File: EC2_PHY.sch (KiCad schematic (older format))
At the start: 72 parts

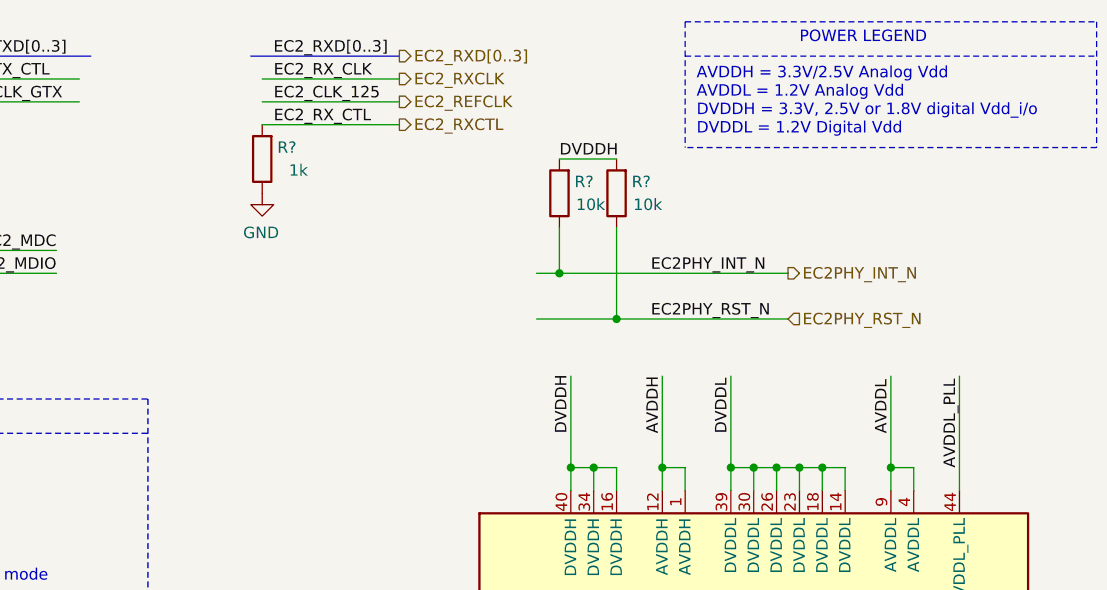
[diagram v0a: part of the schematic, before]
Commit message: Fix reset signal path
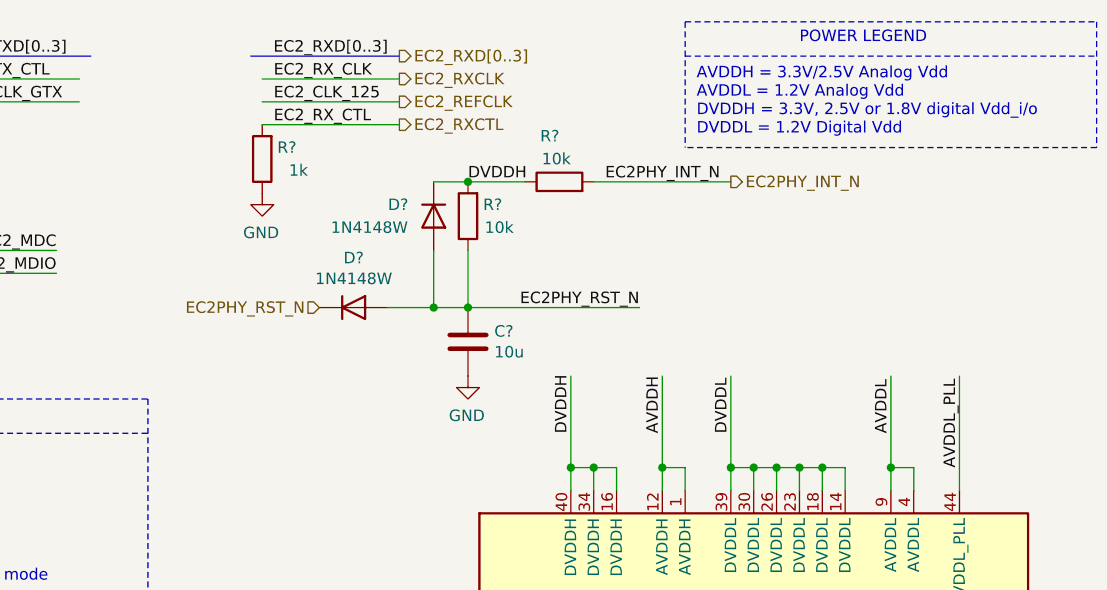
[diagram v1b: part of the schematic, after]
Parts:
- removed R? (x2): 10k, symbol Device:R
- added C?: 10u, symbol Device:C
- added D? (x2): 1N4148W, Diode_SMD:D_SOD-123, symbol Diode:1N4148W
- added R? (x2): 10k, symbol Device:R
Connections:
- wire segments 220 -> 221
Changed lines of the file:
@@
 $Descr A4 11693 8268
 encoding utf-8
-Sheet 16 28
+Sheet 14 28
 Title "DJANGO"
 Date "2020-12-06"
@@
 Text Label 3000 5050 0    50   ~ 0
 EC2PHY_INT_N
-Text Label 4450 1600 0    50   ~ 0
+Text Label 4250 1200 0    50   ~ 0
 EC2PHY_INT_N
-Text HLabel 5050 1600 2    50   Output ~ 0
+Text HLabel 4800 1200 2    50   Output ~ 0
 EC2PHY_INT_N
 Text Label 3000 5350 0    50   ~ 0
 EC2PHY_RST_N
-$Comp
-L Device:R R?
-U 1 1 602C75A3
-P 4050 1250
-AR Path="/5FC823B8/602C75A3" Ref="R?"  Part="1"
-AR Path="/5FD29175/602C75A3" Ref="R?"  Part="1"
-AR Path="/60A03338/602C75A3" Ref="R?"  Part="1"
-F 0 "R?" H 3900 1200 50  0000 L CNN
-F 1 "10k" H 3850 1300 50  0000 L CNN
-F 2 "" V 3980 1250 50  0001 C CNN
-F 3 "~" H 4050 1250 50  0001 C CNN
-	1    4050 1250
-	-1   0    0    1
-$EndComp
-$Comp
-L Device:R R?
-U 1 1 602C75A4
-P 4300 1250
-AR Path="/5FC823B8/602C75A4" Ref="R?"  Part="1"
-AR Path="/5FD29175/602C75A4" Ref="R?"  Part="1"
-AR Path="/60A03338/602C75A4" Ref="R?"  Part="1"
-F 0 "R?" H 4150 1200 50  0000 L CNN
-F 1 "10k" H 4100 1300 50  0000 L CNN
-F 2 "" V 4230 1250 50  0001 C CNN
-F 3 "~" H 4300 1250 50  0001 C CNN
-	1    4300 1250
-	-1   0    0    1
-$EndComp
-Wire Wire Line
-	4300 1100 4050 1100
 Wire Wire Line
 	3000 5350 3600 5350
 Wire Wire Line
 	3000 5050 3600 5050
-Text Label 4450 1800 0    50   ~ 0
+Text Label 4400 1750 2    50   ~ 0
 EC2PHY_RST_N
-Text HLabel 5050 1800 2    50   Input ~ 0
+Text HLabel 3000 1750 0    50   Input ~ 0
 EC2PHY_RST_N
-Wire Wire Line
-	3950 1600 4050 1600
-Wire Wire Line
-	3950 1800 4300 1800
-Wire Wire Line
-	4050 1400 4050 1600
-Connection ~ 4050 1600
-Wire Wire Line
-	4050 1600 5050 1600
-Wire Wire Line
-	4300 1400 4300 1800
-Connection ~ 4300 1800
-Wire Wire Line
-	4300 1800 5050 1800
 Text Label 10600 2200 0    50   ~ 0
 AVDDL
@@
 AVDDH
 Text Label 8500 2950 0    50   ~ 0
-DVDDH
-Text Label 4050 1100 0    50   ~ 0
 DVDDH
 Text Label 4100 2300 1    50   ~ 0
@@
 Wire Wire Line
 	8600 950  8600 800
+$Comp
+L Device:R R?
+U 1 1 6076C7CF
+P 4050 1200
+AR Path="/5FC823B8/6076C7CF" Ref="R?"  Part="1"
+AR Path="/5FD29175/6076C7CF" Ref="R?"  Part="1"
+AR Path="/60A03338/6076C7CF" Ref="R?"  Part="1"
+F 0 "R?" V 4250 1200 50  0000 L CNN
+F 1 "10k" V 4150 1150 50  0000 L CNN
+F 2 "" V 3980 1200 50  0001 C CNN
+F 3 "~" H 4050 1200 50  0001 C CNN
+	1    4050 1200
+	0    -1   -1   0
+$EndComp
+$Comp
+L Device:R R?
+U 1 1 6076C7D5
+P 3650 1350
+AR Path="/5FC823B8/6076C7D5" Ref="R?"  Part="1"
+AR Path="/5FD29175/6076C7D5" Ref="R?"  Part="1"
+AR Path="/60A03338/6076C7D5" Ref="R?"  Part="1"
+F 0 "R?" H 3500 1300 50  0000 L CNN
+F 1 "10k" H 3450 1400 50  0000 L CNN
+F 2 "" V 3580 1350 50  0001 C CNN
+F 3 "~" H 3650 1350 50  0001 C CNN
+	1    3650 1350
+	-1   0    0    1
+$EndComp
+Wire Wire Line
+	3900 1200 3650 1200
+Wire Wire Line
+	3300 1750 3500 1750
+Wire Wire Line
+	4200 1200 4800 1200
+Wire Wire Line
+	3650 1500 3650 1750
+Connection ~ 3650 1750
+Wire Wire Line
+	3650 1750 4400 1750
+Text Label 3650 1200 0    50   ~ 0
+DVDDH
+$Comp
+L Device:C C?
+U 1 1 6076C7E5
+P 3650 1900
+AR Path="/5FC823B8/6076C7E5" Ref="C?"  Part="1"
+AR Path="/5FD29175/6076C7E5" Ref="C?"  Part="1"
+AR Path="/60A03338/6076C7E5" Ref="C?"  Part="1"
+F 0 "C?" H 3765 1946 50  0000 L CNN
+F 1 "10u" H 3765 1855 50  0000 L CNN
+F 2 "" H 3688 1750 50  0001 C CNN
+F 3 "~" H 3650 1900 50  0001 C CNN
+	1    3650 1900
+	1    0    0    -1
+$EndComp
+$Comp
+L power:GND #PWR?
+U 1 1 6076C7EB
+P 3650 2050
+AR Path="/5FC823B8/6076C7EB" Ref="#PWR?"  Part="1"
+AR Path="/5FD29175/6076C7EB" Ref="#PWR?"  Part="1"
+AR Path="/60A03338/6076C7EB" Ref="#PWR?"  Part="1"
+F 0 "#PWR?" H 3650 1800 50  0001 C CNN
+F 1 "GND" H 3655 1877 50  0000 C CNN
+F 2 "" H 3650 2050 50  0001 C CNN
+F 3 "" H 3650 2050 50  0001 C CNN
+	1    3650 2050
+	-1   0    0    -1
+$EndComp
+$Comp
+L Diode:1N4148W D?
+U 1 1 6076C7F1
+P 3500 1350
+F 0 "D?" V 3450 1150 50  0000 L CNN
+F 1 "1N4148W" V 3550 900 50  0000 L CNN
+F 2 "Diode_SMD:D_SOD-123" H 3500 1175 50  0001 C CNN
+F 3 "https://www.vishay.com/docs/85748/1n4148w.pdf" H 3500 1350 50  0001 C CNN
+	1    3500 1350
+	0    1    1    0
+$EndComp
+$Comp
+L Diode:1N4148W D?
+U 1 1 6076C7F7
+P 3150 1750
+F 0 "D?" H 3150 1967 50  0000 C CNN
+F 1 "1N4148W" H 3150 1876 50  0000 C CNN
+F 2 "Diode_SMD:D_SOD-123" H 3150 1575 50  0001 C CNN
+F 3 "https://www.vishay.com/docs/85748/1n4148w.pdf" H 3150 1750 50  0001 C CNN
+	1    3150 1750
+	1    0    0    -1
+$EndComp
+Wire Wire Line
+	3500 1500 3500 1750
+Connection ~ 3500 1750
+Wire Wire Line
+	3500 1750 3650 1750
+Wire Wire Line
+	3500 1200 3650 1200
+Connection ~ 3650 1200
 $EndSCHEMATC
